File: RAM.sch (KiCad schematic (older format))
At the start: 169 parts, among them J2 JTAG_01x06, J3 Conn_01x03_Male, U10 W25Q128JVS, U11 TPS62823DLC, U12 TPS62823DLC, U13 TPS62823DLC, U14 TPS62823DLC, U15 TPS62823DLC, U16 TPS62823DLC, U2 XC7K160T-FFG676, U3 IS43TR16512B-125KBLI, U4 IS43TR16512B-125KBLI, U5 TPS51200DRC, U6 KSZ9031RNXCA, U7 TUSB1310ZAY, U8 TC358778XBG, U9 SiI9022A, Y1 ABM8G-25.000MHZ-18-D2Y-T, Y2 ABM8G-20.000MHZ-18-D2Y-T

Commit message: more routing, bunch of fpga bypass caps, logo
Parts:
- removed R35: R_Small, Resistor_SMD:R_0402_1005Metric, symbol Device:R_Small
- added C37, C38, C39, C40, C41, C42, C60, C61, C68: 100uF, Capacitor_SMD:C_1206_3216Metric, symbol Device:C_Small
- added C43, C44, C45, C46, C47, C48, C49, C50, C51, C56, C57, C58, C59, C69, C75: 4.7uF, Capacitor_SMD:C_0402_1005Metric, symbol Device:C_Small
- added C52, C53, C54, C55: 47uF, Capacitor_SMD:C_1206_3216Metric, symbol Device:C_Small
- added C62, C64, C65, C66: 220uF, Capacitor_SMD:C_1210_3225Metric, symbol Device:C_Small
- added C63, C67: 10uF, Capacitor_SMD:C_0402_1005Metric, symbol Device:C_Small
- added C70, C71, C72, C73, C74: 0.1uF, Capacitor_SMD:C_0402_1005Metric, symbol Device:C_Small
- added GFX?: MountingHole, footprints:mnt-kx7000, symbol Mechanical:MountingHole
- added U17: Si52112-B6, Package_DFN_QFN:TDFN-8-1EP_3x2mm_P0.5mm_EP1.3x1.4mm, symbol reform2-som:Si52112-B6
- J2: footprint (none) -> Connector_PinHeader_1.00mm:PinHeader_1x06_P1.00mm_Horizontal
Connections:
- net +1V0: now also C12.1, L2.2, R36.1, C47.2, C48.2, C49.2, C50.2, C51.2, C56.2, C57.2, C58.2, C59.2, C62.2, C63.1, C64.2, C65.2, C66.2, C67.1, C68.2
- net +1V5: now also C60.2, C61.2
- net +1V8: now also C37.2, C38.2, C41.2, C42.2, C43.2, C44.2, C45.2, C46.2, C52.2, C53.2, C54.2, C55.2
- net +3V3: now also C39.2, C40.2, C74.2, C75.2, U17.1 (VDD)
- net +5V: now also U12.1 (EN), C69.2
- net DISP1_DE: now also U2.D10 (IO_L12N_T1_MRCC_16); no longer U2.F14 (IO_L15P_T2_DQS_16)
- net DISP1_HS: now also U2.D11 (IO_L14N_T2_SRCC_16); no longer U2.E11 (IO_L14P_T2_SRCC_16)
- net DISP1_RGB0: now also U2.E10 (IO_L12P_T1_MRCC_16); no longer U2.D10 (IO_L12N_T1_MRCC_16)
- net DISP1_RGB1: now also U2.D8 (IO_L8N_T1_16); no longer U2.E10 (IO_L12P_T1_MRCC_16)
- net DISP1_RGB10: now also U2.D9 (IO_L8P_T1_16); no longer U2.F8 (IO_L7N_T1_16)
- net DISP1_RGB11: now also U2.F14 (IO_L15P_T2_DQS_16); no longer U2.F9 (IO_L7P_T1_16)
- net DISP1_RGB2: now also U2.F9 (IO_L7P_T1_16); no longer U2.F10 (IO_L11N_T1_SRCC_16)
- net DISP1_RGB3: now also U2.F8 (IO_L7N_T1_16); no longer U2.G11 (IO_L11P_T1_SRCC_16)
- net DISP1_RGB4: now also U2.A9 (IO_L9P_T1_DQS_16); no longer U2.B9 (IO_L10N_T1_16)
- net DISP1_RGB5: now also U2.A8 (IO_L9N_T1_DQS_16); no longer U2.C9 (IO_L10P_T1_16)
- net DISP1_RGB6: now also U2.B9 (IO_L10N_T1_16); no longer U2.A8 (IO_L9N_T1_DQS_16)
- net DISP1_RGB7: now also U2.F10 (IO_L11N_T1_SRCC_16); no longer U2.A9 (IO_L9P_T1_DQS_16)
- net DISP1_RGB8: now also U2.G11 (IO_L11P_T1_SRCC_16); no longer U2.D8 (IO_L8N_T1_16)
- net DISP1_RGB9: now also U2.C9 (IO_L10P_T1_16); no longer U2.D9 (IO_L8P_T1_16)
- net DISP1_VS: now also U2.E11 (IO_L14P_T2_SRCC_16); no longer U2.D11 (IO_L14N_T2_SRCC_16)
- net GND: now also C37.1, C38.1, C39.1, C40.1, C41.1, C42.1, C43.1, C44.1, C45.1, C46.1, C47.1, C48.1, C49.1, C50.1, C51.1, C52.1, C53.1, C54.1, C55.1, C56.1, C57.1, C58.1, C59.1, C60.1, C61.1, C62.1, C63.2, C64.1, C65.1, C66.1, C67.2, C68.1, C69.1, C74.1, C75.1, U17.4 (VSS)
- net PCIE1_CLK_N: now also U17.8 (~DIFF2)
- net PCIE1_CLK_P: now also U17.7 (DIFF2)
- net PCIE2_CLK_N: now also C73.1
- net PCIE2_CLK_P: now also C72.1
- net at U2.D5 (MGTREFCLK0N_116): now also C71.2
- net at U2.D6 (MGTREFCLK0P_116): now also C70.2
- net at U2.F5 (MGTREFCLK1N_116): now also C73.2
- net at U2.F6 (MGTREFCLK1P_116): now also C72.2
- new net PCIE1_CLK_HOST_N: C71.1, U17.6 (~DIFF1)
- new net PCIE1_CLK_HOST_P: C70.1, U17.5 (DIFF1)
- no-connect marks 22 -> 46
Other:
- note added: "TODO: 25mhz input"
- note added: "TODO: caps needed?"
- note removed: "TODO: 2x 10uF"
- note removed: "TODO: PCIe clocking"
- moved on the sheet: TP1, TP2, TP3, TP4, TP5, TP6, U2H

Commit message: schematics: add many decoupling caps
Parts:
- added C100, C102, C110, C111, C112, C113, C114, C115, C116, C117, C118, C119, C120, C121, C122, C123, C124, C125, C126, C127, C128, C129, C130, C131, C132, C133, C134, C135, C136, C137, C138, C139, C140, C141, C142, C143, C144, C145, C146, C147, C148, C149, C150, C151, C152, C153, C154, C155, C156, C157, C158, C159, C160, C161, C162, C163, C164, C165, C167, C168, C169, C170, C171, C172, C173, C174, C175, C176, C177, C178, C180, C181, C182, C183, C184, C185, C186, C188, C83, C84, C85, C86, C87, C88, C90, C91, C92, C95, C96, C99: 0.1uF, Capacitor_SMD:C_0402_1005Metric, symbol Device:C_Small
- added C101, C76, C77, C79, C80, C81, C82, C89, C93, C94, C97, C98: 10uF, Capacitor_SMD:C_0402_1005Metric, symbol Device:C_Small
- added C103: 10nF, Capacitor_SMD:C_0402_1005Metric, symbol Device:C_Small
- added C104, C105, C106, C107, C108, C109, C78: 4.7uF, Capacitor_SMD:C_0402_1005Metric, symbol Device:C_Small
- added C166, C179, C187: 1uF, Capacitor_SMD:C_0402_1005Metric, symbol Device:C_Small
- added FB1, FB2, FB3: Ferrite_Bead_Small, Inductor_SMD:L_0603_1608Metric, symbol Device:Ferrite_Bead_Small
- added R35: 0, Resistor_SMD:R_0603_1608Metric, symbol Device:R_Small
- added R95: 4.7k, Resistor_SMD:R_0402_1005Metric, symbol Device:R_Small
- added R96: 5.1k, Resistor_SMD:R_0402_1005Metric, symbol Device:R_Small
- added R97: 10k, Resistor_SMD:R_0402_1005Metric, symbol Device:R_Small
- added R98: 100, Resistor_SMD:R_0402_1005Metric, symbol Device:R_Small
- C67: value 10uF -> 4.7uF
- R32, R38, R41, R44, R47: value R_Small -> 0; footprint Resistor_SMD:R_0402_1005Metric -> Resistor_SMD:R_0603_1608Metric
- TP1, TP10, TP11, TP12, TP2, TP3, TP4, TP5, TP6, TP7, TP8, TP9: footprint (none) -> TestPoint:TestPoint_Pad_1.0x1.0mm
- gave numbers to parts that had none: 1
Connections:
- net +1V0: now also C106.2, C107.2, R35.1; no longer C12.1, C63.1, C67.1, L2.2, R36.1
- net +1V1: now also C166.1, C167.1, C168.1, C169.1, C170.1, C171.1, C172.1, C173.1, C174.1, C175.1, C176.1, C177.1, C178.1
- net +1V2: now also U2.M5 (MGTAVTTRCAL_115), U9.60 (AVCC12), C104.2, C105.2, C110.1, C111.1, C112.1, C113.1, C114.1, C115.1, C116.1, C117.1, C121.1, C122.1, C123.1, C124.1, C125.1, C82.2, C83.2, C84.2, C85.2, C86.2, C87.2, C88.2, C97.2, FB2.2, FB3.2, R98.2
- net +1V5: now also C130.1, C131.1, C132.1, C133.1, C134.1, C135.1, C136.1, C137.1, C138.1, C139.1, C140.1, C141.1, C142.1, C143.1, C144.1, C145.1, C146.1, C147.1, C148.1, C149.1, C150.1, C151.1, C152.1, C153.1, C154.1, C155.1, C156.1, C157.1, C158.1, C159.1, C160.1, C161.1, C162.1, C163.1, C164.1, C165.1
- net +1V8: now also U9.21 (IOVCC), U9.3 (IOVCC), U9.46 (IOVCC), C108.2, C109.2, C118.1, C119.1, C120.1, C126.1, C127.1, C128.1, C129.1, C179.1, C180.1, C181.1, C182.1, C183.1, C184.1, C185.1, C186.1
- net +3V3: now also C187.1, C188.1, C89.2, C90.2, C91.2, C92.2, C93.2, FB1.2, R95.1
- net +5V: now also C67.2, C78.2; no longer U12.1 (EN)
- net ETH_MDIO: now also R95.2
- net GND: now also C67.1, U9.43 (CGND), U9.55 (RSVDL), U9.69 (IO_SEL), U9.70 (VDDQ), U9.73 (TP), C100.1, C101.1, C102.1, C103.1, C104.1, C105.1, C106.1, C107.1, C108.1, C109.1, C110.2, C111.2, C112.2, C113.2, C114.2, C115.2, C116.2, C117.2, C118.2, C119.2, C120.2, C121.2, C122.2, C123.2, C124.2, C125.2, C126.2, C127.2, C128.2, C129.2, C130.2, C131.2, C132.2, C133.2, C134.2, C135.2, C136.2, C137.2, C138.2, C139.2, C140.2, C141.2, C142.2, C143.2, C144.2, C145.2, C146.2, C147.2, C148.2, C149.2, C150.2, C151.2, C152.2, C153.2, C154.2, C155.2, C156.2, C157.2, C158.2, C159.2, C160.2, C161.2, C162.2, C163.2, C164.2, C165.2, C166.2, C167.2, C168.2, C169.2, C170.2, C171.2, C172.2, C173.2, C174.2, C175.2, C176.2, C177.2, C178.2, C179.2, C180.2, C181.2, C182.2, C183.2, C184.2, C185.2, C186.2, C187.2, C188.2, C76.2, C77.2, C78.1, C79.2, C80.2, C81.2, C82.1, C83.1, C84.1, C85.1, C86.1, C87.1, C88.1, C89.1, C90.1, C91.1, C92.1, C93.1, C94.1, C95.1, C96.1, C97.1, C98.1, C99.1, R96.1, R97.2; no longer C67.2
- net HDMI_CEC: now also U9.50 (CEC_D)
- net HDMI_HPD: now also U9.54 (HPD), R97.1
- net HDMI_SCL: now also U9.49 (DSCL)
- net HDMI_SDA: now also U9.48 (DSDA)
- net at U2.M6 (MGTRREF_115): now also R98.1
- net DISP1_SCL: now reaches U9.1 (CSCL)
- net DISP1_SDA: now reaches U9.2 (CSDA)
- net at U9.56 (EXT_SWING): now also R96.2
- net at C11.1, L1.2, R32.2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: now also C79.1
- net at C13.1, L3.2, R38.2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: now also C76.1
- net at C14.1, L4.2, R41.2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: now also C80.1
- net at C15.1, L5.2, R44.2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: now also C77.1
- net at C16.1, L6.2, R47.2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: now also C81.1
- net ETH_VDDA: now reaches U6.1 (AVDDH)
- net ETH_VDDA: now also U6.12 (AVDDH), C94.2, C95.2, C96.2, FB1.1
- net ETH_VDDL: now reaches U6.4 (AVDDL)
- net ETH_VDDL: now also U6.9 (AVDDL), C100.2, C98.2, C99.2, FB2.1
- net ETH_VDDL_PLL: now reaches U6.44 (AVDDL_PLL)
- net ETH_VDDL_PLL: now also C101.2, C102.2, C103.2, FB3.1
- new net: C12.1, C63.1, L2.2, R35.2, R36.1
- no-connect marks 46 -> 48
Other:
- note added: "2x DDR3 decoupling caps"
- note added: "DVDDH decoupling"
- note added: "DVDDL decoupling"
- note added: "TODO: bead"
- note added: "TODO: double check CI2CA"
- note added: "TODO: enables? power sequencing?"
- note added: "TODO: move USB to 115?"
- note added: "TODO: read errata again (pullup on out_enable etc)"
- note added: "TODO: series Rs?"
- note added: "note: 40mhz is supposed to\nwork only with SSC"
- note removed: "TODO: 10uF"
- note removed: "TODO: up to 40MHz"
- moved on the sheet: C31, C32, C33, C34, C35, C36, C63, C74, C75, R32, R38, R41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

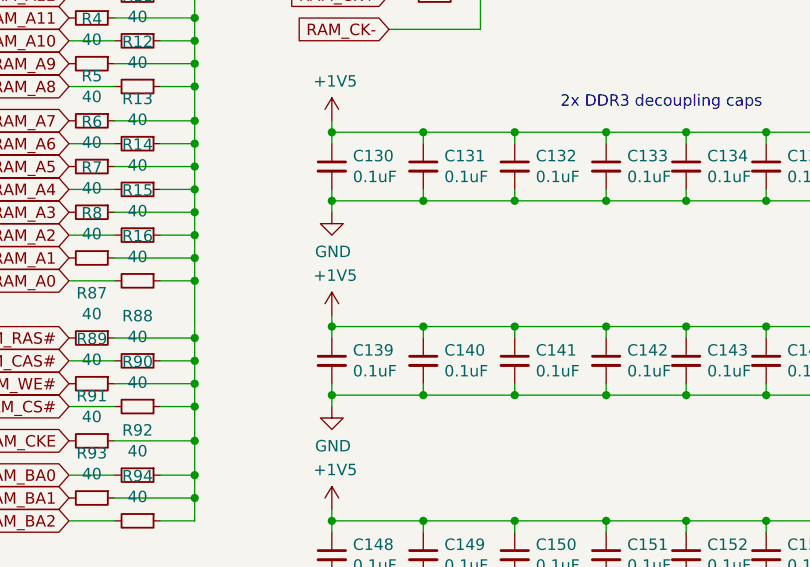
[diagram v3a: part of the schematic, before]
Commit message: ram bypass caps placed
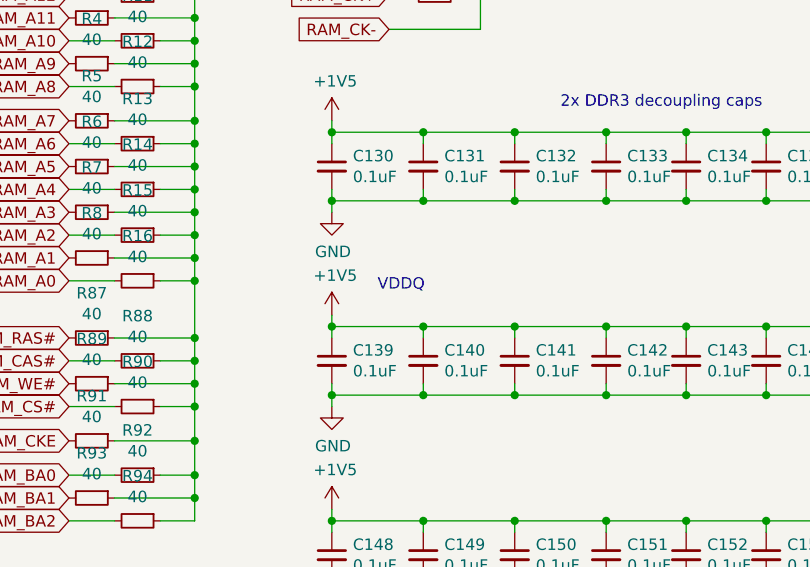
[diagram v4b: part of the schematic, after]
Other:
- note added: "VDDQ"
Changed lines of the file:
@@
 Wire Wire Line
 	27750 3350 27750 3400
+Text Notes 10450 14600 0    50   ~ 0
+VDDQ
 $EndSCHEMATC

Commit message: place lots of caps; place some power supplies
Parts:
- removed C117: 0.1uF, Capacitor_SMD:C_0402_1005Metric, symbol Device:C_Small
- added C? (x3): 4.7uF, Capacitor_SMD:C_0402_1005Metric, symbol Device:C_Small
- J3: footprint (none) -> Connector_PinHeader_2.00mm:PinHeader_1x03_P2.00mm_Horizontal
- Y1, Y2: footprint (none) -> Crystal:Crystal_SMD_3225-4Pin_3.2x2.5mm
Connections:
- net +5V: now also C?.2, C?.2, C?.2
- net GND: now also Y1.4, C?.1, C?.1, C?.1
- net TUSB_VSSOSC: now also Y2.4
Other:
- note removed: "TODO: 4.7uF"
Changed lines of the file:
@@
 F 0 "Y1" H 38894 12696 50  0000 L CNN
 F 1 "ABM8G-25.000MHZ-18-D2Y-T" H 38894 12605 50  0000 L CNN
-F 2 "" H 38750 12650 50  0001 C CNN
+F 2 "Crystal:Crystal_SMD_3225-4Pin_3.2x2.5mm" H 38750 12650 50  0001 C CNN
 F 3 "~" H 38750 12650 50  0001 C CNN
 	1    38750 12650
@@
 	39150 12950 39150 13050
 Wire Wire Line
-	39150 13050 38750 13050
+	39150 13050 38900 13050
 Wire Wire Line
 	39150 12750 39150 12650
@@
 F 0 "Y2" H 8294 20846 50  0000 L CNN
 F 1 "ABM8G-20.000MHZ-18-D2Y-T" H 8294 20755 50  0000 L CNN
-F 2 "" H 8150 20800 50  0001 C CNN
+F 2 "Crystal:Crystal_SMD_3225-4Pin_3.2x2.5mm" H 8150 20800 50  0001 C CNN
 F 3 "~" H 8150 20800 50  0001 C CNN
 	1    8150 20800
@@
 	8550 21100 8550 21200
 Wire Wire Line
-	8550 21200 8150 21200
+	8550 21200 8300 21200
 Connection ~ 8150 21200
 Wire Wire Line
@@
 F 0 "J3" H 16372 19232 50  0000 R CNN
 F 1 "Conn_01x03_Male" H 16372 19323 50  0000 R CNN
-F 2 "" H 16400 19300 50  0001 C CNN
+F 2 "Connector_PinHeader_2.00mm:PinHeader_1x03_P2.00mm_Horizontal" H 16400 19300 50  0001 C CNN
 F 3 "~" H 16400 19300 50  0001 C CNN
 	1    16400 19300
@@
 	1    0    0    -1
 $EndComp
-Text Notes 25200 1750 0    50   ~ 0
-TODO: 4.7uF
-Text Notes 29100 1700 0    50   ~ 0
-TODO: 4.7uF
-Text Notes 29100 3450 0    50   ~ 0
-TODO: 4.7uF
-Text Notes 32900 1650 0    50   ~ 0
-TODO: 4.7uF
-Text Notes 32900 3450 0    50   ~ 0
-TODO: 4.7uF
 Wire Wire Line
 	19150 2650 19150 3000
@@
 	1    0    0    -1
 $EndComp
-$Comp
-L Device:C_Small C117
-U 1 1 7C66E5C9
-P 26150 13500
-F 0 "C117" H 26242 13546 50  0000 L CNN
-F 1 "0.1uF" H 26242 13455 50  0000 L CNN
-F 2 "Capacitor_SMD:C_0402_1005Metric" H 26150 13500 50  0001 C CNN
-F 3 "~" H 26150 13500 50  0001 C CNN
-	1    26150 13500
-	1    0    0    -1
-$EndComp
 Text Notes 23400 12900 0    50   ~ 0
 TODO: bead
 Wire Wire Line
 	23550 13350 23950 13350
-Wire Wire Line
-	26150 13350 26150 13400
 Connection ~ 23550 13350
 Wire Wire Line
@@
 Wire Wire Line
 	25800 13400 25800 13350
-Connection ~ 25800 13350
-Wire Wire Line
-	25800 13350 26150 13350
 Wire Wire Line
 	25450 13350 25450 13400
@@
 Wire Wire Line
 	23550 13650 23950 13650
-Wire Wire Line
-	26150 13650 26150 13600
 Connection ~ 23550 13650
 Wire Wire Line
@@
 Wire Wire Line
 	25800 13600 25800 13650
-Connection ~ 25800 13650
-Wire Wire Line
-	25800 13650 26150 13650
 Wire Wire Line
 	25450 13600 25450 13650
@@
 Text Notes 10450 14600 0    50   ~ 0
 VDDQ
+Wire Wire Line
+	8150 20700 8150 20600
+Wire Wire Line
+	8150 20600 8300 20600
+Wire Wire Line
+	8300 20600 8300 21200
+Connection ~ 8300 21200
+Wire Wire Line
+	8300 21200 8150 21200
+Wire Wire Line
+	38750 12550 38750 12500
+Wire Wire Line
+	38750 12500 38900 12500
+Wire Wire Line
+	38900 12500 38900 13050
+Connection ~ 38900 13050
+Wire Wire Line
+	38900 13050 38750 13050
+$Comp
+L Device:C_Small C?
+U 1 1 630C5C72
+P 33150 1800
+F 0 "C?" V 32921 1800 50  0000 C CNN
+F 1 "4.7uF" V 33012 1800 50  0000 C CNN
+F 2 "Capacitor_SMD:C_0402_1005Metric" H 33150 1800 50  0001 C CNN
+F 3 "~" H 33150 1800 50  0001 C CNN
+	1    33150 1800
+	1    0    0    1
+$EndComp
+Connection ~ 33150 1700
+$Comp
+L power:GND #PWR?
+U 1 1 630C63BB
+P 33150 1900
+F 0 "#PWR?" H 33150 1650 50  0001 C CNN
+F 1 "GND" H 33155 1727 50  0000 C CNN
+F 2 "" H 33150 1900 50  0001 C CNN
+F 3 "" H 33150 1900 50  0001 C CNN
+	1    33150 1900
+	1    0    0    -1
+$EndComp
+$Comp
+L Device:C_Small C?
+U 1 1 630C685D
+P 29400 3600
+F 0 "C?" V 29171 3600 50  0000 C CNN
+F 1 "4.7uF" V 29262 3600 50  0000 C CNN
+F 2 "Capacitor_SMD:C_0402_1005Metric" H 29400 3600 50  0001 C CNN
+F 3 "~" H 29400 3600 50  0001 C CNN
+	1    29400 3600
+	1    0    0    1
+$EndComp
+Connection ~ 29400 3500
+$Comp
+L Device:C_Small C?
+U 1 1 630C6F0A
+P 33150 3500
+F 0 "C?" V 32921 3500 50  0000 C CNN
+F 1 "4.7uF" V 33012 3500 50  0000 C CNN
+F 2 "Capacitor_SMD:C_0402_1005Metric" H 33150 3500 50  0001 C CNN
+F 3 "~" H 33150 3500 50  0001 C CNN
+	1    33150 3500
+	1    0    0    1
+$EndComp
+Connection ~ 33150 3400
+$Comp
+L power:GND #PWR?
+U 1 1 630C9AF2
+P 29400 3700
+F 0 "#PWR?" H 29400 3450 50  0001 C CNN
+F 1 "GND" H 29405 3527 50  0000 C CNN
+F 2 "" H 29400 3700 50  0001 C CNN
+F 3 "" H 29400 3700 50  0001 C CNN
+	1    29400 3700
+	1    0    0    -1
+$EndComp
+$Comp
+L power:GND #PWR?
+U 1 1 630C9F5C
+P 33150 3600
+F 0 "#PWR?" H 33150 3350 50  0001 C CNN
+F 1 "GND" H 33155 3427 50  0000 C CNN
+F 2 "" H 33150 3600 50  0001 C CNN
+F 3 "" H 33150 3600 50  0001 C CNN
+	1    33150 3600
+	1    0    0    -1
+$EndComp
 $EndSCHEMATC

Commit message: place all components
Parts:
- removed C88: 0.1uF, Capacitor_SMD:C_0402_1005Metric, symbol Device:C_Small
- gave numbers to parts that had none: 3
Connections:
- net SD2_CD: now also U2.A10 (IO_L22N_T3_16); no longer U2.A12 (IO_L24N_T3_16)
- net SD2_DATA2: now also U2.A12 (IO_L24N_T3_16); no longer U2.A10 (IO_L22N_T3_16)
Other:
- note added: "TODO: 0603"
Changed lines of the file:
@@
 Text GLabel 12800 6600 0    50   BiDi ~ 0
 SD2_DATA3
-Text GLabel 12800 6500 0    50   BiDi ~ 0
+Text GLabel 12800 6900 0    50   BiDi ~ 0
 SD2_DATA2
 Text GLabel 12800 6400 0    50   BiDi ~ 0
@@
 Text GLabel 11300 3200 2    50   Output ~ 0
 UART1_TX
-Text GLabel 12800 6900 0    50   Input ~ 0
+Text GLabel 12800 6500 0    50   Input ~ 0
 SD2_CD
 Text GLabel 11300 3400 2    50   Input ~ 0
@@
 	1    0    0    1
 $EndComp
-$Comp
-L Device:C_Small C88
-U 1 1 913C8059
-P 42600 7650
-F 0 "C88" V 42371 7650 50  0000 C CNN
-F 1 "0.1uF" V 42462 7650 50  0000 C CNN
-F 2 "Capacitor_SMD:C_0402_1005Metric" H 42600 7650 50  0001 C CNN
-F 3 "~" H 42600 7650 50  0001 C CNN
-	1    42600 7650
-	1    0    0    1
-$EndComp
 Wire Wire Line
 	41900 7500 42250 7500
 Wire Wire Line
 	42250 7500 42250 7550
-Wire Wire Line
-	42250 7500 42600 7500
-Wire Wire Line
-	42600 7500 42600 7550
-Connection ~ 42250 7500
 Connection ~ 41900 7500
 $Comp
@@
 Wire Wire Line
 	40500 7800 40850 7800
-Wire Wire Line
-	42600 7800 42600 7750
 Connection ~ 40500 7800
 Wire Wire Line
@@
 Wire Wire Line
 	42250 7750 42250 7800
-Connection ~ 42250 7800
-Wire Wire Line
-	42250 7800 42600 7800
 Wire Wire Line
 	41900 7750 41900 7800
@@
 	38900 13050 38750 13050
 $Comp
-L Device:C_Small C?
+L Device:C_Small C117
 U 1 1 630C5C72
 P 33150 1800
-F 0 "C?" V 32921 1800 50  0000 C CNN
+F 0 "C117" V 32921 1800 50  0000 C CNN
 F 1 "4.7uF" V 33012 1800 50  0000 C CNN
 F 2 "Capacitor_SMD:C_0402_1005Metric" H 33150 1800 50  0001 C CNN
@@
 Connection ~ 33150 1700
 $Comp
-L power:GND #PWR?
+L power:GND #PWR0179
 U 1 1 630C63BB
 P 33150 1900
-F 0 "#PWR?" H 33150 1650 50  0001 C CNN
+F 0 "#PWR0179" H 33150 1650 50  0001 C CNN
 F 1 "GND" H 33155 1727 50  0000 C CNN
 F 2 "" H 33150 1900 50  0001 C CNN
@@
 $EndComp
 $Comp
-L Device:C_Small C?
+L Device:C_Small C190
 U 1 1 630C685D
 P 29400 3600
-F 0 "C?" V 29171 3600 50  0000 C CNN
+F 0 "C190" V 29171 3600 50  0000 C CNN
 F 1 "4.7uF" V 29262 3600 50  0000 C CNN
 F 2 "Capacitor_SMD:C_0402_1005Metric" H 29400 3600 50  0001 C CNN
@@
 Connection ~ 29400 3500
 $Comp
-L Device:C_Small C?
+L Device:C_Small C189
 U 1 1 630C6F0A
 P 33150 3500
-F 0 "C?" V 32921 3500 50  0000 C CNN
+F 0 "C189" V 32921 3500 50  0000 C CNN
 F 1 "4.7uF" V 33012 3500 50  0000 C CNN
 F 2 "Capacitor_SMD:C_0402_1005Metric" H 33150 3500 50  0001 C CNN
@@
 Connection ~ 33150 3400
 $Comp
-L power:GND #PWR?
+L power:GND #PWR0180
 U 1 1 630C9AF2
 P 29400 3700
-F 0 "#PWR?" H 29400 3450 50  0001 C CNN
+F 0 "#PWR0180" H 29400 3450 50  0001 C CNN
 F 1 "GND" H 29405 3527 50  0000 C CNN
 F 2 "" H 29400 3700 50  0001 C CNN
@@
 $EndComp
 $Comp
-L power:GND #PWR?
+L power:GND #PWR0181
 U 1 1 630C9F5C
 P 33150 3600
-F 0 "#PWR?" H 33150 3350 50  0001 C CNN
+F 0 "#PWR0181" H 33150 3350 50  0001 C CNN
 F 1 "GND" H 33155 3427 50  0000 C CNN
 F 2 "" H 33150 3600 50  0001 C CNN
@@
 	1    0    0    -1
 $EndComp
+Text Notes 41650 10850 0    50   ~ 0
+TODO: 0603
+Text Notes 39950 10950 0    50   ~ 0
+TODO: 0603
+Text Notes 39800 10050 0    50   ~ 0
+TODO: 0603
+Text Notes 41600 9700 0    50   ~ 0
+TODO: 0603
+Text Notes 39950 8450 0    50   ~ 0
+TODO: 0603
+Text Notes 39950 7500 0    50   ~ 0
+TODO: 0603
 $EndSCHEMATC

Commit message: more routing
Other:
- note added: "TODO: double check,\nreally 3v3?"
- note added: "TODO: double check.\nkinda weird locations."
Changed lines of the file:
@@
 Text Notes 39950 7500 0    50   ~ 0
 TODO: 0603
+Text Notes 16000 14650 0    50   ~ 0
+TODO: double check.\nkinda weird locations.
+Text Notes 18550 15700 0    50   ~ 0
+TODO: double check,\nreally 3v3?
 $EndSCHEMATC

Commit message: more routing
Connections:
- net DISP1_RGB10: now also U2.G14 (IO_L5N_T0_16); no longer U2.D9 (IO_L8P_T1_16)
- net DISP1_RGB11: now also U2.F10 (IO_L11N_T1_SRCC_16); no longer U2.F14 (IO_L15P_T2_DQS_16)
- net DISP1_RGB12: now also U2.H14 (IO_L5P_T0_16); no longer U2.H11 (IO_L6N_T0_VREF_16)
- net DISP1_RGB13: now also U2.G11 (IO_L11P_T1_SRCC_16); no longer U2.H12 (IO_L6P_T0_16)
- net DISP1_RGB14: now also U2.H11 (IO_L6N_T0_VREF_16); no longer U2.G14 (IO_L5N_T0_16)
- net DISP1_RGB15: now also U2.G9 (IO_L2N_T0_16); no longer U2.H14 (IO_L5P_T0_16)
- net DISP1_RGB16: now also U2.H13 (IO_L3N_T0_DQS_16); no longer U2.J10 (IO_L4N_T0_16)
- net DISP1_RGB17: now also U2.G10 (IO_L2P_T0_16); no longer U2.J11 (IO_L4P_T0_16)
- net DISP1_RGB18: now also U2.J13 (IO_L3P_T0_DQS_16); no longer U2.H13 (IO_L3N_T0_DQS_16)
- net DISP1_RGB19: now also U2.H12 (IO_L6P_T0_16); no longer U2.J13 (IO_L3P_T0_DQS_16)
- net DISP1_RGB20: now also U2.J10 (IO_L4N_T0_16); no longer U2.G9 (IO_L2N_T0_16)
- net DISP1_RGB21: now also U2.H8 (IO_L1N_T0_16); no longer U2.G10 (IO_L2P_T0_16)
- net DISP1_RGB22: now also U2.H9 (IO_L1P_T0_16); no longer U2.H8 (IO_L1N_T0_16)
- net DISP1_RGB23: now also U2.J11 (IO_L4P_T0_16); no longer U2.H9 (IO_L1P_T0_16)
- net DISP1_RGB7: now also U2.D9 (IO_L8P_T1_16); no longer U2.F10 (IO_L11N_T1_SRCC_16)
- net DISP1_RGB8: now also U2.F14 (IO_L15P_T2_DQS_16); no longer U2.G11 (IO_L11P_T1_SRCC_16)
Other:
- note removed: "TODO: connector"
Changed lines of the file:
@@
 Text GLabel 12800 4100 0    50   Input ~ 0
 DISP1_RGB6
-Text GLabel 12800 4300 0    50   Input ~ 0
+Text GLabel 12800 3600 0    50   Input ~ 0
 DISP1_RGB7
-Text GLabel 12800 4200 0    50   Input ~ 0
+Text GLabel 12800 5000 0    50   Input ~ 0
 DISP1_RGB8
 Text GLabel 12800 4000 0    50   Input ~ 0
 DISP1_RGB9
-Text GLabel 12800 3600 0    50   Input ~ 0
+Text GLabel 12800 3100 0    50   Input ~ 0
 DISP1_RGB10
-Text GLabel 12800 5000 0    50   Input ~ 0
+Text GLabel 12800 4300 0    50   Input ~ 0
 DISP1_RGB11
-Text GLabel 12800 3300 0    50   Input ~ 0
+Text GLabel 12800 3000 0    50   Input ~ 0
 DISP1_RGB12
-Text GLabel 12800 3200 0    50   Input ~ 0
+Text GLabel 12800 4200 0    50   Input ~ 0
 DISP1_RGB13
-Text GLabel 12800 3100 0    50   Input ~ 0
+Text GLabel 12800 3300 0    50   Input ~ 0
 DISP1_RGB14
-Text GLabel 12800 3000 0    50   Input ~ 0
+Text GLabel 12800 2500 0    50   Input ~ 0
 DISP1_RGB15
-Text GLabel 12800 2900 0    50   Input ~ 0
+Text GLabel 12800 2700 0    50   Input ~ 0
 DISP1_RGB16
-Text GLabel 12800 2800 0    50   Input ~ 0
+Text GLabel 12800 2400 0    50   Input ~ 0
 DISP1_RGB17
-Text GLabel 12800 2700 0    50   Input ~ 0
-DISP1_RGB18
-Text GLabel 12800 2600 0    50   Input ~ 0
+Text GLabel 12800 3200 0    50   Input ~ 0
 DISP1_RGB19
-Text GLabel 12800 2500 0    50   Input ~ 0
-DISP1_RGB20
-Text GLabel 12800 2400 0    50   Input ~ 0
-DISP1_RGB21
 Text GLabel 12800 2300 0    50   Input ~ 0
-DISP1_RGB22
+DISP1_RGB21
 Text GLabel 12800 2200 0    50   Input ~ 0
+DISP1_RGB22
+Text GLabel 12800 2800 0    50   Input ~ 0
 DISP1_RGB23
 Text GLabel 12800 4800 0    50   Output ~ 0
@@
 Text GLabel 16800 4600 2    50   Output ~ 0
 DISP2_PCLK
-Text Notes 30550 13450 0    50   ~ 0
-TODO: connector
 $Comp
 L reform-kintex-rescue:TUSB1310ZAY-TUSB1310ZAY U7
@@
 Text Notes 18550 15700 0    50   ~ 0
 TODO: double check,\nreally 3v3?
+Text GLabel 12800 2600 0    50   Input ~ 0
+DISP1_RGB18
+Text GLabel 12800 2900 0    50   Input ~ 0
+DISP1_RGB20
 $EndSCHEMATC
